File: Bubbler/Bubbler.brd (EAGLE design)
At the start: 95.2 x 63.5 mm, 73 parts, among them SW1 SWITCH-DIP-GDH-02, SW2 ITT-SWITCH-KSS-G, U1 STM32F41X-100P, U2 SPANSION-S25FL256, U3 LM4890, U4 BIPOLAR-PMBT6428, U5 USBLC6-2, U6 TLV1117, U7 MOLEX-1.25-WTB-RA-CONN-2POS, X2 CM415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

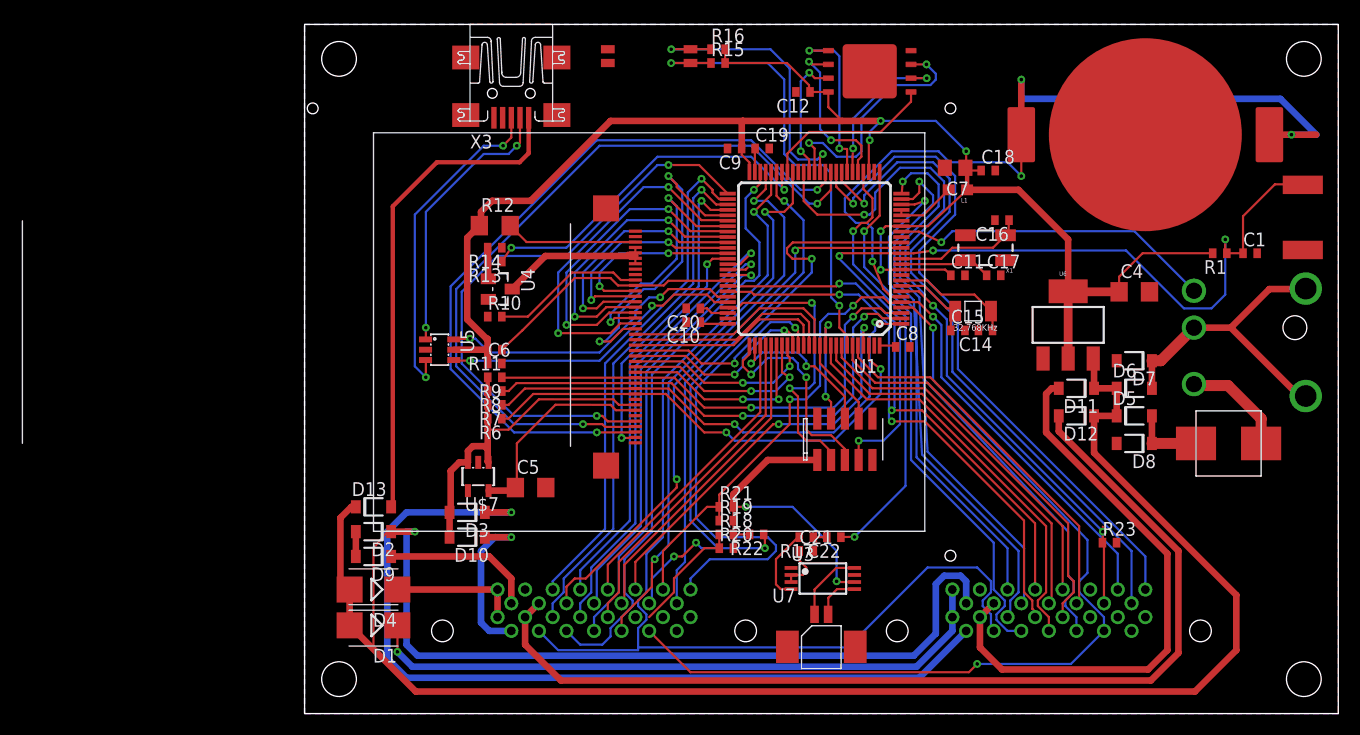
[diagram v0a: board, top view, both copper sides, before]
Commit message: Corrected expansion connectors
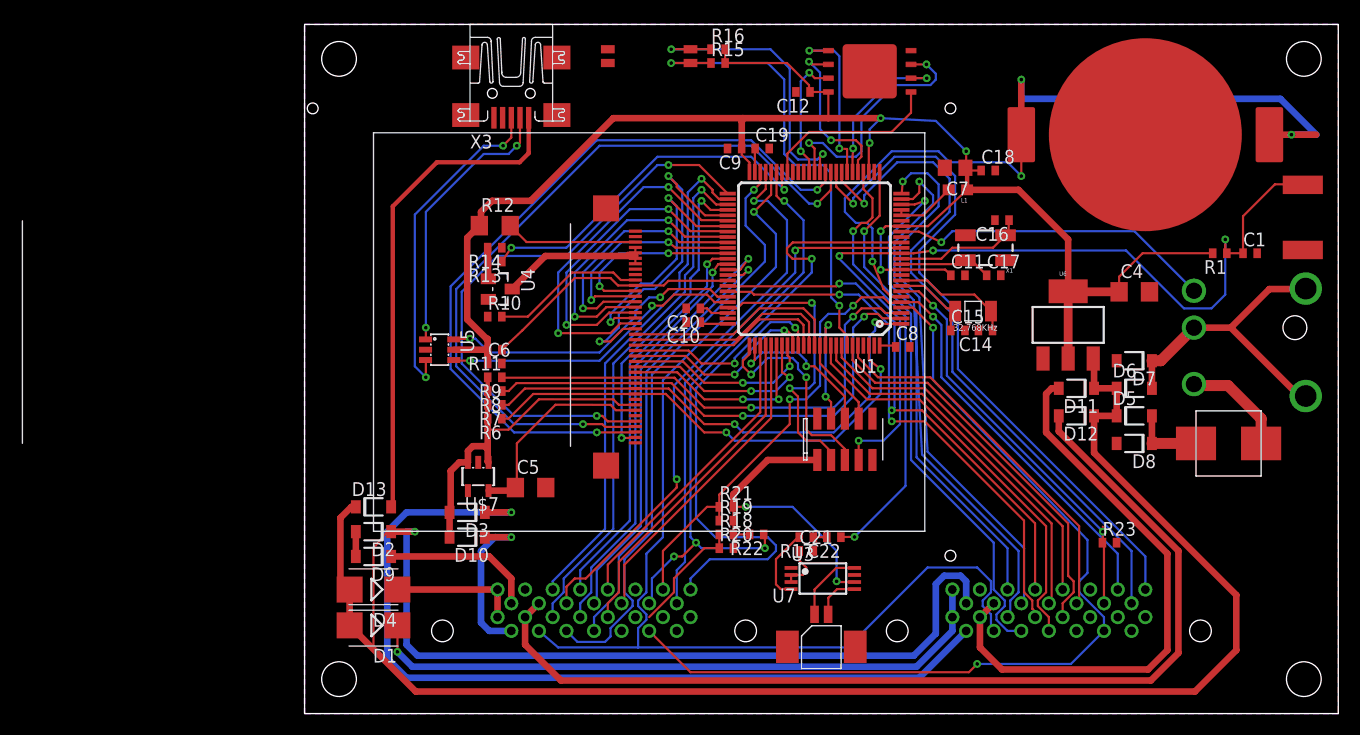
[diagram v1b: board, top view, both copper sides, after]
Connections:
- new net CARD0_ID: CARD0.P22, U1.17
- new net CARD1_ID: CARD1.P22, U1.97
- net EXT0_11: no longer U1.40
- net EXT1_11: no longer U1.42
- net EXT1_12: no longer U1.41, U1.97
- net GND: no longer CARD0.P22, CARD1.P22
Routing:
- net EXT0_11: track 69.2 -> 0.00 mm, vias 1 -> 0
- net EXT1_11: track 50.5 -> 0.00 mm, vias 2 -> 0
- net EXT1_12: track 37.8 -> 0.00 mm, vias 2 -> 0
- net EXT1_5: track 42.8 -> 38.5 mm
- net CARD1_INSERT: track 56.9 -> 55.6 mm
- net FLASH_CS: track 16.0 -> 16.5 mm
